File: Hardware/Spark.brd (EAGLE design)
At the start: 40.3 x 45.7 mm, 8 parts

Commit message: initial firmware
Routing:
- net GND: track 86.6 -> 88.8 mm
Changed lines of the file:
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@@
 <wire x1="11.35" y1="5.08" x2="16.51" y2="5.08" width="0.8128" layer="16"/>
 <wire x1="16.51" y1="5.08" x2="22.86" y2="11.43" width="0.8128" layer="16"/>
-<wire x1="11.35" y1="5.08" x2="11.35" y2="11.51" width="0.8128" layer="16"/>
-<wire x1="11.35" y1="11.51" x2="2.54" y2="20.32" width="0.8128" layer="16"/>
+<wire x1="11.35" y1="5.08" x2="11.35" y2="12.78" width="0.8128" layer="16"/>
 <wire x1="22.86" y1="11.43" x2="27.94" y2="16.51" width="0.4064" layer="1"/>
 <polygon width="0.4064" layer="1" isolate="0.4064">
@@
 <vertex x="-1.27" y="-1.27"/>
 </polygon>
+<wire x1="11.35" y1="12.78" x2="7.62" y2="16.51" width="0.8128" layer="16"/>
+<wire x1="7.62" y1="16.51" x2="3.81" y2="16.51" width="0.8128" layer="16"/>
+<wire x1="3.81" y1="16.51" x2="2.54" y2="17.78" width="0.8128" layer="16"/>
+<wire x1="2.54" y1="17.78" x2="2.54" y2="20.32" width="0.8128" layer="16"/>
 </signal>
 <signal name="VCC">

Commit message: begin v2
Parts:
- removed JP2, JP3: (no value), pinhead:1X04
- removed U$1: TEENSY_3.1_BASIC, Teensy_3_Series_Board_v1.0:TEENSY_3.1_BASIC
- added C1, C2, C3, C4, C5: 0.1uF, SparkFun-Capacitors:0603-CAP
- added C6, C7: 10uF, SparkFun-Capacitors:1210
- added L1: 3.3uH, SparkFun-Passives:0805
- added Q2: MMBT4403, SparkFun-DiscreteSemi:SOT23-3
- added R2: 8.2K, SparkFun-Resistors:0603-RES
- added R3, R4: 100, SparkFun-Resistors:0603-RES
- added R5: 20k, SparkFun-Resistors:0603-RES
- added U1: HX711, Testing:SO16
- JP4: device pinhead:1X03 -> SparkFun-Connectors:1X05
- moved JP4 43.6 mm to (27.9, -22.9)
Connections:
- removed net 3.3V: JP2.3, JP3.1, JP4.1, U$1.3.3V, U$1.3.3V1
- removed net AGND: U$1.AGND
- removed net CLK: JP3.3, U$1.3
- removed net RX: JP2.2, U$1.0
- removed net TX: JP2.1, U$1.1
- removed net TX2: JP4.3, U$1.10
- removed net VBAT: U$1.VBAT
- removed net VIN: U$1.VIN
- new net A+: JP4.2, R4.1
- new net A-: JP4.3, R3.1
- new net AVDD: C3.1, C7.1, JP4.5, L1.1
- new net N$10: U1.16
- new net N$3: C1.1, R3.2, U1.7
- new net N$4: Q2.1, U1.2
- new net N$5: L1.2, Q2.3, R5.2, U1.3
- new net N$6: R2.2, R5.1, U1.4
- new net N$7: C2.2, U1.6
- new net N$8: C1.2, R4.2, U1.8
- new net SCK: U1.11
- new net VDD: C4.1
- net DAT: now also U1.12; no longer JP3.2, U$1.2
- net GND: now also C2.1, C3.2, C4.2, C5.2, C6.2, C7.2, JP4.1, JP4.4, R2.1, U1.14, U1.15, U1.5; no longer JP2.4, JP3.4, JP4.2, U$1.GND, U$1.GND1
- net IGNITE: no longer U$1.4
- net VCC: now also C5.1, C6.1, Q2.2, U1.1
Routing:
- net 3.3V: track 69.1 -> 0.00 mm
- net GND: track 88.8 -> 53.6 mm
- net DAT: track 11.0 -> 0.00 mm
- net CLK: track 10.3 -> 0.00 mm
- net TX2: track 8.45 -> 0.00 mm
- net RX: track 6.88 -> 0.00 mm
- net TX: track 6.88 -> 0.00 mm
- net IGNITE: track 33.9 -> 30.4 mm

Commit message: 7-segment and arduino
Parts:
- added J1: ARDUINO_R3_SHIELD, SparkFun-Boards:UNO_R3_SHIELD
- added R10, R11, R12, R13, R6, R7, R8, R9: 100, SparkFun:0402-RES
- added U$1: 7-SEGMENT-4DIGIT-COUNTERPTH, SparkFun-Displays:7-SEGMENT-4DIGIT-COUNTER
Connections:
- removed net DAT: U1.12
- new net A: J1.D5, R6.2
- new net B: J1.D6, R7.2
- new net C: J1.D7, R8.2
- new net D: J1.D8, R9.2
- new net DATA: J1.D3, U1.12
- new net DIG1: J1.D13, U$1.12
- new net DIG2: J1.A0, U$1.9
- new net DIG3: J1.A1, U$1.8
- new net DIG4: J1.A2, U$1.6
- new net DP: J1.D12, R13.2
- new net E: J1.D9, R10.2
- new net F: J1.D10, R11.2
- new net G: J1.D11, R12.2
- new net N$11: R6.1, U$1.11
- new net N$12: R7.1, U$1.7
- new net N$14: R8.1, U$1.4
- new net N$15: R9.1, U$1.2
- new net N$16: R10.1, U$1.1
- new net N$17: R11.1, U$1.10
- new net N$18: R12.1, U$1.5
- new net N$19: R13.1, U$1.3
- new net VIN: J1.VIN, JP1.2, JP5.1
- net IGNITE: now also J1.D4
- net SCK: now also J1.D2
- net VCC: now also J1.5V; no longer JP1.2, JP5.1
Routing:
- net VCC: track 22.4 -> 0.00 mm
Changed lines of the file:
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@@
 <attribute name="PROD_ID" value="CAP-08604" x="-13.97" y="-121.92" size="1.778" layer="27" display="off"/>
 </element>
+<element name="J1" library="SparkFun-Boards" package="UNO_R3_SHIELD" value="ARDUINO_R3_SHIELD" x="-55.88" y="-22.86"/>
+<element name="U$1" library="SparkFun-Displays" package="7-SEGMENT-4DIGIT-COUNTER" value="7-SEGMENT-4DIGIT-COUNTERPTH" x="-24.13" y="-53.34"/>
+<element name="R6" library="SparkFun" package="0402-RES" value="100" x="-54.61" y="-68.58"/>
+<element name="R7" library="SparkFun" package="0402-RES" value="100" x="-50.8" y="-68.58"/>
+<element name="R8" library="SparkFun" package="0402-RES" value="100" x="-46.99" y="-68.58"/>
+<element name="R9" library="SparkFun" package="0402-RES" value="100" x="-43.18" y="-68.58"/>
+<element name="R10" library="SparkFun" package="0402-RES" value="100" x="-39.37" y="-68.58"/>
+<element name="R11" library="SparkFun" package="0402-RES" value="100" x="-35.56" y="-68.58"/>
+<element name="R12" library="SparkFun" package="0402-RES" value="100" x="-31.75" y="-68.58"/>
+<element name="R13" library="SparkFun" package="0402-RES" value="100" x="-27.94" y="-68.58"/>
 </elements>
 <signals>
@@
 <wire x1="30.48" y1="17.78" x2="24.13" y2="24.13" width="0.4064" layer="16"/>
 <wire x1="24.13" y1="24.13" x2="19.05" y2="24.13" width="0.4064" layer="16"/>
+<contactref element="J1" pad="D4"/>
+<wire x1="-53.34" y1="21.59" x2="19.05" y2="24.13" width="0" layer="19" extent="16-16"/>
 </signal>
 <signal name="GND">
@@
 </signal>
 <signal name="VCC">
-<contactref element="JP1" pad="2"/>
-<contactref element="JP5" pad="1"/>
-<wire x1="6.35" y1="5.08" x2="8.89" y2="2.54" width="0.8128" layer="1"/>
-<wire x1="8.89" y1="2.54" x2="24.13" y2="2.54" width="0.8128" layer="1"/>
-<wire x1="24.13" y1="2.54" x2="26.59" y2="5" width="0.8128" layer="1"/>
-<wire x1="26.59" y1="5" x2="26.59" y2="5.08" width="0.8128" layer="1"/>
 <contactref element="C6" pad="1"/>
 <contactref element="Q2" pad="2"/>
 <contactref element="C5" pad="1"/>
 <contactref element="U1" pad="1"/>
+<contactref element="J1" pad="5V"/>
 <wire x1="11.11" y1="-30.21" x2="-0.33" y2="-38.1" width="0" layer="19" extent="1-1"/>
 <wire x1="1.905" y1="-18.04" x2="11.11" y2="-30.21" width="0" layer="19" extent="1-1"/>
 <wire x1="30.9" y1="-34.29" x2="11.11" y2="-30.21" width="0" layer="19" extent="1-1"/>
-<wire x1="8.89" y1="2.54" x2="1.905" y2="-18.04" width="0" layer="19" extent="1-1"/>
+<wire x1="-5.08" y1="6.35" x2="1.905" y2="-18.04" width="0" layer="19" extent="1-1"/>
 </signal>
 <signal name="N$2">
@@
 <wire x1="24.13" y1="7.62" x2="35.56" y2="7.62" width="0.8128" layer="1"/>
 </signal>
-<signal name="DAT">
+<signal name="DATA">
 <contactref element="U1" pad="12"/>
+<contactref element="J1" pad="D3"/>
+<wire x1="6.985" y1="-12.44" x2="-53.34" y2="24.13" width="0" layer="19" extent="1-1"/>
 </signal>
 <signal name="SCK">
 <contactref element="U1" pad="11"/>
+<contactref element="J1" pad="D2"/>
+<wire x1="8.255" y1="-12.44" x2="-53.34" y2="26.67" width="0" layer="19" extent="1-1"/>
 </signal>
 <signal name="N$4">
@@
 <contactref element="U1" pad="16"/>
 </signal>
+<signal name="DIG4">
+<contactref element="U$1" pad="6"/>
+<contactref element="J1" pad="A2"/>
+<wire x1="-5.08" y1="24.13" x2="-17.78" y2="-64.3382" width="0" layer="19" extent="1-1"/>
+</signal>
+<signal name="DIG3">
+<contactref element="U$1" pad="8"/>
+<contactref element="J1" pad="A1"/>
+<wire x1="-5.08" y1="21.59" x2="-20.32" y2="-42.3418" width="0" layer="19" extent="1-1"/>
+</signal>
+<signal name="DIG2">
+<contactref element="U$1" pad="9"/>
+<contactref element="J1" pad="A0"/>
+<wire x1="-5.08" y1="19.05" x2="-22.86" y2="-42.3418" width="0" layer="19" extent="1-1"/>
+</signal>
+<signal name="DIG1">
+<contactref element="U$1" pad="12"/>
+<contactref element="J1" pad="D13"/>
+<wire x1="-53.34" y1="-2.54" x2="-30.48" y2="-42.3418" width="0" layer="19" extent="1-1"/>
+</signal>
+<signal name="G">
+<contactref element="R12" pad="2"/>
+<contactref element="J1" pad="D11"/>
+<wire x1="-53.34" y1="2.54" x2="-31.1" y2="-68.58" width="0" layer="19" extent="1-1"/>
+</signal>
+<signal name="E">
+<contactref element="R10" pad="2"/>
+<contactref element="J1" pad="D9"/>
+<wire x1="-53.34" y1="7.62" x2="-38.72" y2="-68.58" width="0" layer="19" extent="1-1"/>
+</signal>
+<signal name="D">
+<contactref element="R9" pad="2"/>
+<contactref element="J1" pad="D8"/>
+<wire x1="-53.34" y1="10.16" x2="-42.53" y2="-68.58" width="0" layer="19" extent="1-1"/>
+</signal>
+<signal name="B">
+<contactref element="R7" pad="2"/>
+<contactref element="J1" pad="D6"/>
+<wire x1="-53.34" y1="16.51" x2="-50.15" y2="-68.58" width="0" layer="19" extent="1-1"/>
+</signal>
+<signal name="A">
+<contactref element="R6" pad="2"/>
+<contactref element="J1" pad="D5"/>
+<wire x1="-53.34" y1="19.05" x2="-53.96" y2="-68.58" width="0" layer="19" extent="1-1"/>
+</signal>
+<signal name="DP">
+<contactref element="R13" pad="2"/>
+<contactref element="J1" pad="D12"/>
+<wire x1="-53.34" y1="0" x2="-27.29" y2="-68.58" width="0" layer="19" extent="1-1"/>
+</signal>
+<signal name="N$11">
+<contactref element="U$1" pad="11"/>
+<contactref element="R6" pad="1"/>
+<wire x1="-27.94" y1="-42.3418" x2="-55.26" y2="-68.58" width="0" layer="19" extent="1-1"/>
+</signal>
+<signal name="N$12">
+<contactref element="U$1" pad="7"/>
+<contactref element="R7" pad="1"/>
+<wire x1="-17.78" y1="-42.3418" x2="-51.45" y2="-68.58" width="0" layer="19" extent="1-1"/>
+</signal>
+<signal name="N$14">
+<contactref element="U$1" pad="4"/>
+<contactref element="R8" pad="1"/>
+<wire x1="-22.86" y1="-64.3382" x2="-47.64" y2="-68.58" width="0" layer="19" extent="1-1"/>
+</signal>
+<signal name="N$15">
+<contactref element="U$1" pad="2"/>
+<contactref element="R9" pad="1"/>
+<wire x1="-27.94" y1="-64.3382" x2="-43.83" y2="-68.58" width="0" layer="19" extent="1-1"/>
+</signal>
+<signal name="N$16">
+<contactref element="U$1" pad="1"/>
+<contactref element="R10" pad="1"/>
+<wire x1="-30.48" y1="-64.3382" x2="-40.02" y2="-68.58" width="0" layer="19" extent="1-1"/>
+</signal>
+<signal name="N$17">
+<contactref element="U$1" pad="10"/>
+<contactref element="R11" pad="1"/>
+<wire x1="-25.4" y1="-42.3418" x2="-36.21" y2="-68.58" width="0" layer="19" extent="1-1"/>
+</signal>
+<signal name="N$18">
+<contactref element="U$1" pad="5"/>
+<contactref element="R12" pad="1"/>
+<wire x1="-20.32" y1="-64.3382" x2="-32.4" y2="-68.58" width="0" layer="19" extent="1-1"/>
+</signal>
+<signal name="N$19">
+<contactref element="U$1" pad="3"/>
+<contactref element="R13" pad="1"/>
+<wire x1="-25.4" y1="-64.3382" x2="-28.59" y2="-68.58" width="0" layer="19" extent="1-1"/>
+</signal>
+<signal name="C">
+<contactref element="R8" pad="2"/>
+<contactref element="J1" pad="D7"/>
+<wire x1="-53.34" y1="13.97" x2="-46.34" y2="-68.58" width="0" layer="19" extent="1-1"/>
+</signal>
+<signal name="F">
+<contactref element="R11" pad="2"/>
+<contactref element="J1" pad="D10"/>
+<wire x1="-53.34" y1="5.08" x2="-34.91" y2="-68.58" width="0" layer="19" extent="1-1"/>
+</signal>
+<signal name="VIN">
+<contactref element="J1" pad="VIN"/>
+<contactref element="JP1" pad="2"/>
+<contactref element="JP5" pad="1"/>
+<wire x1="6.35" y1="5.08" x2="26.59" y2="5.08" width="0" layer="19" extent="1-1"/>
+<wire x1="-5.08" y1="13.97" x2="6.35" y2="5.08" width="0" layer="19" extent="1-1"/>
+</signal>
 </signals>

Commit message: ground arduino
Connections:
- net GND: now also J1.GND@0, J1.GND@1, J1.GND@2
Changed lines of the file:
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@@
 <contactref element="C4" pad="2"/>
 <contactref element="U1" pad="15"/>
-<wire x1="7.95" y1="-38.1" x2="2.87" y2="-38.1" width="0" layer="19" extent="1-1"/>
+<contactref element="J1" pad="GND@2"/>
+<contactref element="J1" pad="GND@1"/>
+<contactref element="J1" pad="GND@0"/>
+<wire x1="-5.08" y1="8.89" x2="-53.34" y2="-5.08" width="0" layer="19" extent="1-1"/>
+<wire x1="-5.08" y1="11.43" x2="-5.08" y2="8.89" width="0" layer="19" extent="1-1"/>
+<wire x1="2.54" y1="17.78" x2="-5.08" y2="11.43" width="0" layer="19" extent="16-16"/>
+<wire x1="4.445" y1="-12.44" x2="11.35" y2="5.08" width="0" layer="19" extent="1-1"/>
+<wire x1="3.175" y1="-12.44" x2="4.445" y2="-12.44" width="0" layer="19" extent="1-1"/>
+<wire x1="6.985" y1="-18.04" x2="4.445" y2="-12.44" width="0" layer="19" extent="1-1"/>
+<wire x1="7.95" y1="-38.1" x2="6.985" y2="-18.04" width="0" layer="19" extent="1-1"/>
+<wire x1="2.87" y1="-38.1" x2="7.95" y2="-38.1" width="0" layer="19" extent="1-1"/>
 <wire x1="19.47" y1="-34.29" x2="7.95" y2="-38.1" width="0" layer="19" extent="1-1"/>
 <wire x1="24.98" y1="-34.29" x2="19.47" y2="-34.29" width="0" layer="19" extent="1-1"/>
@@
 <wire x1="35.56" y1="-22.86" x2="38.52" y2="-27.94" width="0" layer="19" extent="1-1"/>
 <wire x1="27.94" y1="-22.86" x2="35.56" y2="-22.86" width="0" layer="19" extent="1-1"/>
-<wire x1="6.985" y1="-18.04" x2="7.95" y2="-38.1" width="0" layer="19" extent="1-1"/>
-<wire x1="4.445" y1="-12.44" x2="6.985" y2="-18.04" width="0" layer="19" extent="1-1"/>
-<wire x1="3.175" y1="-12.44" x2="4.445" y2="-12.44" width="0" layer="19" extent="1-1"/>
-<wire x1="11.35" y1="5.08" x2="4.445" y2="-12.44" width="0" layer="19" extent="1-1"/>
 </signal>
 <signal name="VCC">

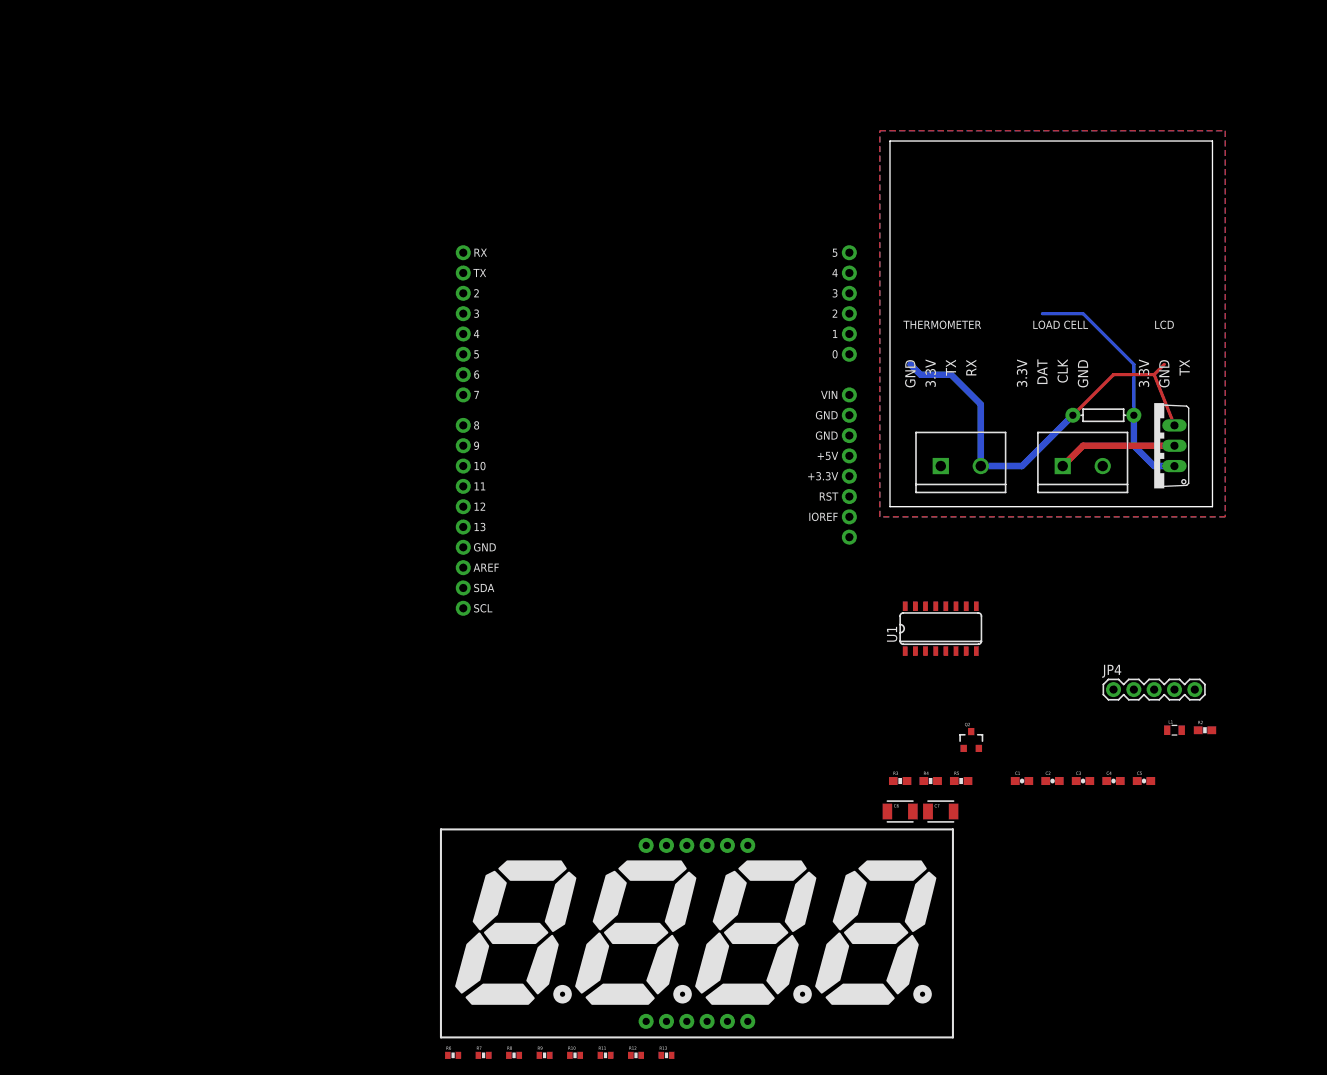
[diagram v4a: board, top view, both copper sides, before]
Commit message: switch to 0805 packages
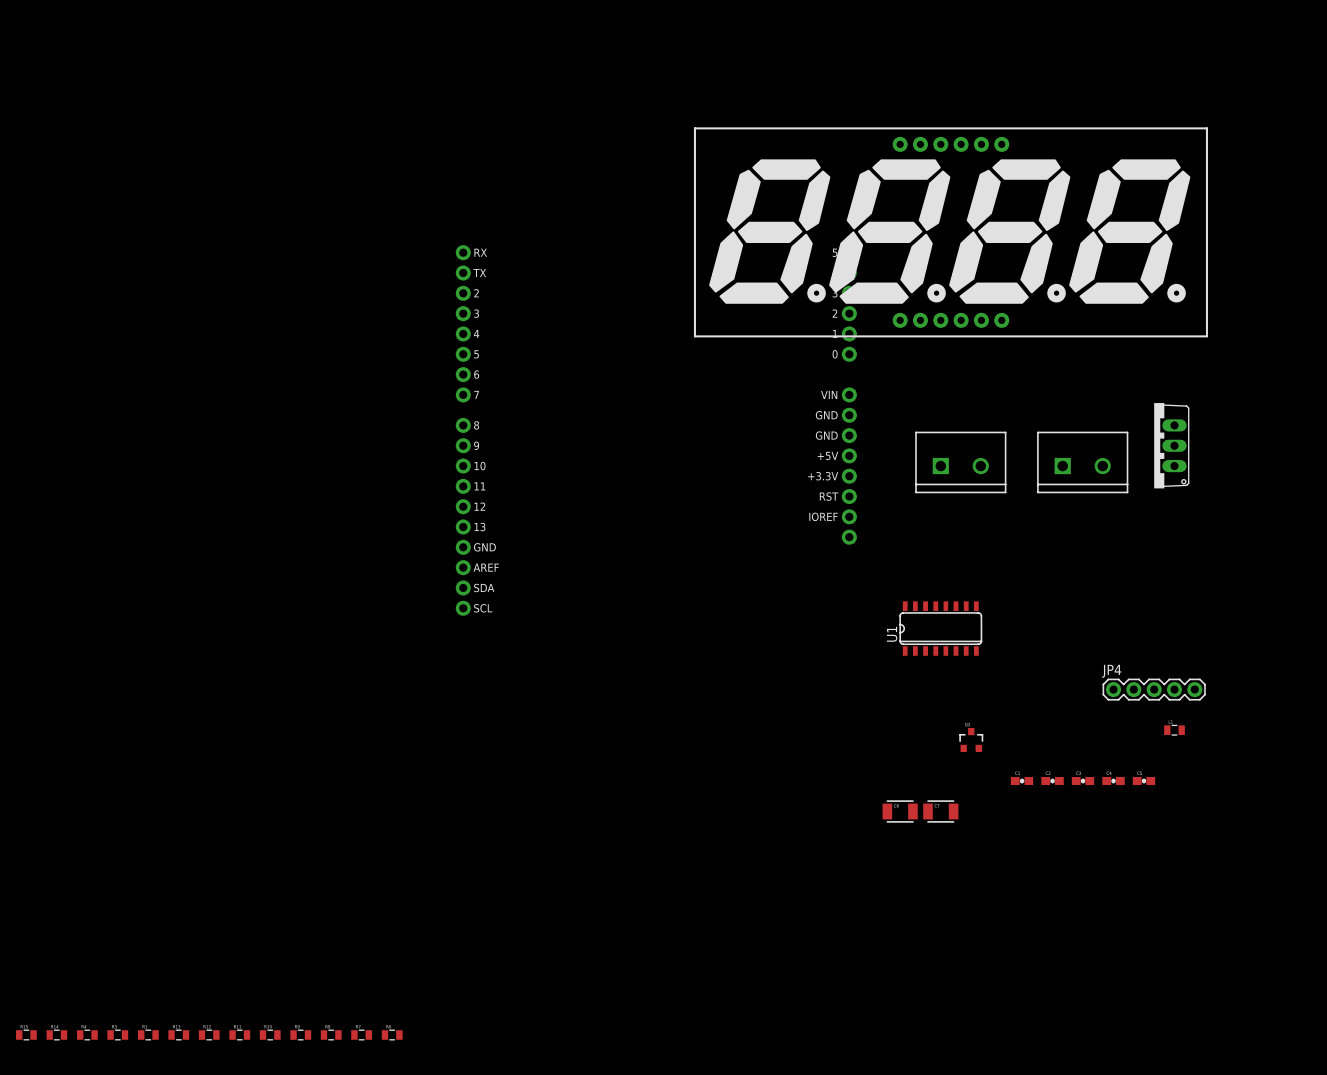
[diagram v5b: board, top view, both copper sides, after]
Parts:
- removed R2: 8.2K, SparkFun-Resistors:0603-RES
- removed R5: 20k, SparkFun-Resistors:0603-RES
- added R14: 8.2k, SparkFun-Resistors:0805
- added R15: 20k, SparkFun-Resistors:0805
- R1: device SparkFun-Passives:AXIAL-0.3EZ -> SparkFun-Resistors:0805
- R10, R11, R12, R13, R6, R7, R8, R9: device SparkFun:0402-RES -> SparkFun-Resistors:0805
- R3, R4: device SparkFun-Resistors:0603-RES -> SparkFun-Resistors:0805
- moved R1 142.3 mm to (-92.7, -66.0)
- moved R4 110.1 mm to (-100.3, -66.0)
- moved R3 102.8 mm to (-96.5, -66.0)
- moved U$1 93.2 mm to (7.62, 34.3)
- moved R13 61.0 mm to (-88.9, -66.0)
- moved R12 53.4 mm to (-85.1, -66.0)
- moved R11 45.8 mm to (-81.3, -66.0)
- moved R10 38.2 mm to (-77.5, -66.0)
- moved R9 30.6 mm to (-73.7, -66.0)
- moved R8 23.0 mm to (-69.8, -66.0)
- moved R7 15.5 mm to (-66.0, -66.0)
- moved R6 8.03 mm to (-62.2, -66.0)
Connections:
- net A: now also R13.1; no longer R6.2
- net B: now also R6.1; no longer R7.2
- net C: now also R7.1; no longer R8.2
- net D: now also R8.1; no longer R9.2
- net DP: now also R12.1; no longer R13.2
- net E: now also R9.1; no longer R10.2
- net F: now also R10.1; no longer R11.2
- net G: now also R11.1; no longer R12.2
- net GND: now also R1.2, R14.1; no longer R1.P$1, R2.1
- net IGNITE: now also R1.1; no longer R1.P$2
- net N$11: now also R13.2; no longer R6.1
- net N$12: now also R6.2; no longer R7.1
- net N$14: now also R7.2; no longer R8.1
- net N$15: now also R8.2; no longer R9.1
- net N$16: now also R9.2; no longer R10.1
- net N$17: now also R10.2; no longer R11.1
- net N$18: now also R11.2; no longer R12.1
- net N$19: now also R12.2; no longer R13.1
- net N$5: now also R15.2; no longer R5.2
- net N$6: now also R14.2, R15.1; no longer R2.2, R5.1
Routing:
- net GND: track 53.6 -> 0.00 mm
- net IGNITE: track 30.4 -> 0.00 mm
- net N$2: track 15.0 -> 0.00 mm
- removed copper zone on layer 1, net GND
- removed copper zone on layer 16, net GND
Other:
- board outline removed
- board text removed: "3.3V DAT CLK GND"
- board text removed: "3.3V GND TX"
- board text removed: "GND 3.3V TX RX"
- board text removed: "LCD"
- board text removed: "LOAD CELL"
- board text removed: "THERMOMETER"

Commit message: begin layout
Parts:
- R1: value (none) -> 10k
- moved R1 152.5 mm to (25.4, 30.5)
- moved R14 152.5 mm to (14.0, 30.5)
- moved R3 152.5 mm to (21.6, 30.5)
- moved R4 152.5 mm to (17.8, 30.5)
- moved R11 138.6 mm to (5.59, 41.9)
- moved R15 132.5 mm to (3.81, 5.08)
- moved R13 131.5 mm to (5.59, 25.4)
- moved R12 127.0 mm to (5.59, 22.9)
- moved R10 125.4 mm to (5.59, 27.9)
- moved R7 125.1 mm to (5.59, 36.6)
- moved R6 125.1 mm to (5.59, 39.1)
- moved R9 124.9 mm to (5.59, 30.5)
- moved R8 124.5 mm to (5.59, 33.0)
- moved J1 60.4 mm to (0.00, 0.00)
- moved JP1 54.6 mm to (44.5, 54.6), turned to 180 degrees
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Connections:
- net A: now also J1.D11; no longer J1.D5
- net D: now also J1.A1; no longer J1.D8
- net DIG3: now also J1.D8; no longer J1.A1
- net G: now also J1.D5; no longer J1.D11
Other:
- board text removed: "+ -"
- board text removed: "10k"
- board text removed: "IGN"
- board text removed: "POWER"
